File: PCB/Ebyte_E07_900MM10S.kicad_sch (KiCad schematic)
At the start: 5 parts, among them U20 ESP32-C3_OLED, U3 Ai-Thinker-Ra-02

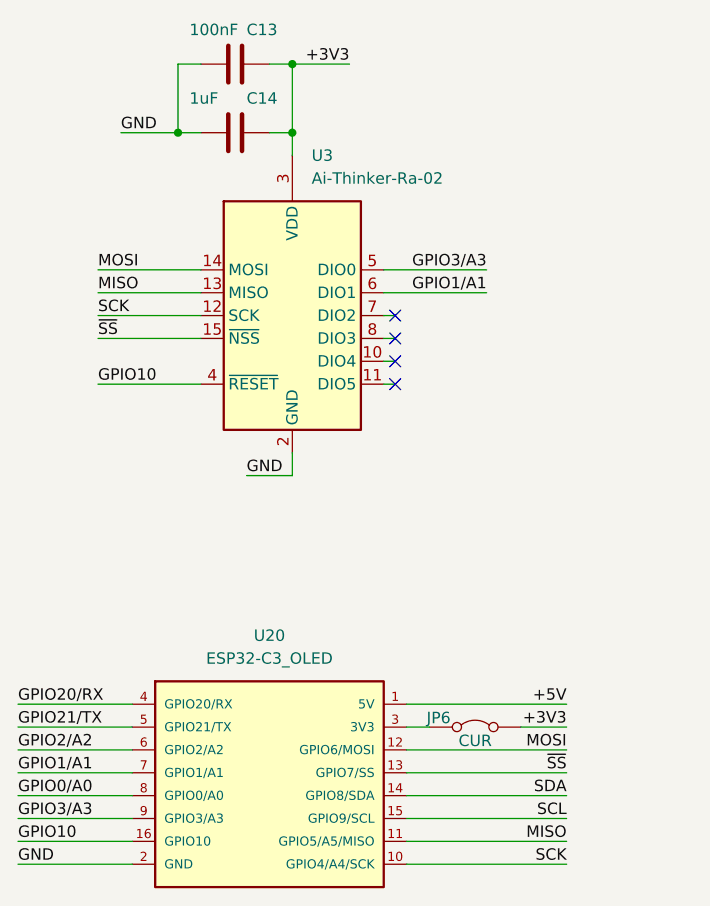
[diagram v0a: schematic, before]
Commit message: Move KiCad files to PCB
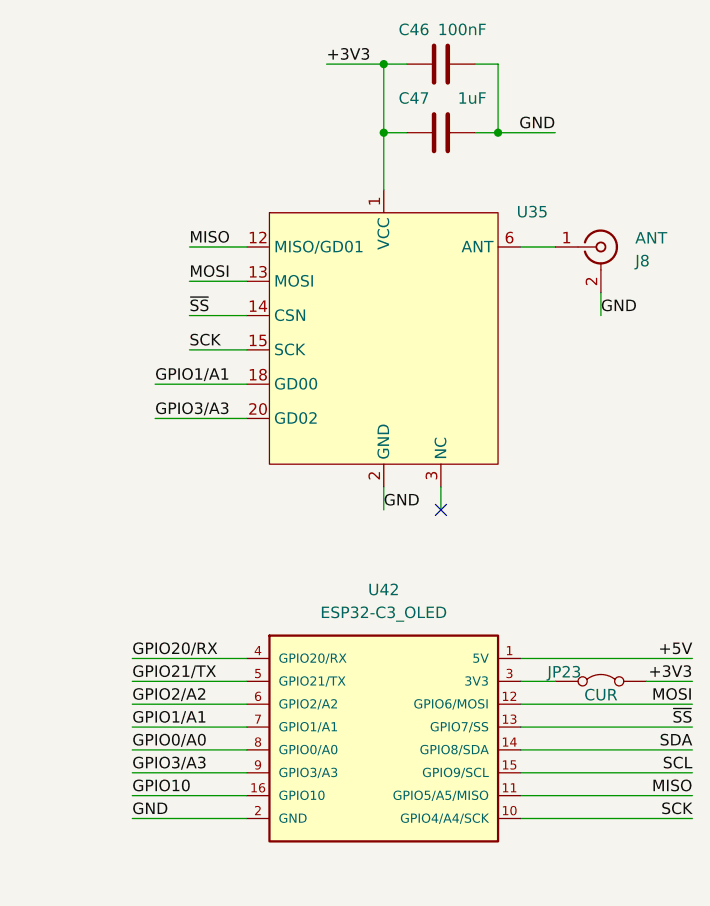
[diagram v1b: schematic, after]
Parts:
- removed C13: 100nF, Capacitor_SMD:C_0603_1608Metric, symbol Device:C
- removed C14: 1uF, Capacitor_SMD:C_0603_1608Metric, symbol Device:C
- removed JP6: CUR, Connector_PinHeader_2.54mm:PinHeader_1x02_P2.54mm_Vertical, symbol Jumper:Jumper_2_Bridged
- removed U20: ESP32-C3_OLED, module_radio:ESP32-C3_OLED, symbol module_radio:ESP32-C3_OLED
- removed U3: Ai-Thinker-Ra-02, RF_Module:Ai-Thinker-Ra-01-LoRa, symbol RF_Module:Ai-Thinker-Ra-02
- added C46: 100nF, Capacitor_SMD:C_0603_1608Metric, symbol Device:C
- added C47: 1uF, Capacitor_SMD:C_0603_1608Metric, symbol Device:C
- added J8: ANT, Connector_Coaxial:SMA_Samtec_SMA-J-P-H-ST-EM1_EdgeMount, symbol Connector:Conn_Coaxial
- added JP23: CUR, Connector_PinHeader_2.54mm:PinHeader_1x02_P2.54mm_Vertical, symbol Jumper:Jumper_2_Bridged
- added U35: Ebyte_E79, module_radio:Ebyte_E07_900MM10S, symbol module_radio:Ebyte_E07_900MM10S
- added U42: ESP32-C3_OLED, module_radio:ESP32-C3_OLED, symbol module_radio:ESP32-C3_OLED
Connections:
- net +3V3: now also C46.1, C47.1, JP23.2 (B), U35.1 (VCC)
- net +5V: now also U42.1 (5V)
- net GND: now also C46.2, C47.2, J8.2 (Ext), U35.16 (GND), U35.2 (GND), U35.7 (GND), U42.2 (GND)
- net GPIO0/A0: now also U42.8 (GPIO0/A0)
- net GPIO1/A1: now also U42.7 (GPIO1/A1)
- net GPIO10: now also U42.16 (GPIO10)
- net GPIO1/A1: now also U35.18 (GD00)
- net GPIO2/A2: now also U42.6 (GPIO2/A2)
- net GPIO20/RX: now also U42.4 (GPIO20/RX)
- net GPIO21/TX: now also U42.5 (GPIO21/TX)
- net GPIO3/A3: now also U35.20 (GD02), U42.9 (GPIO3/A3)
- net MISO: now also U35.12 (MISO/GD01), U42.11 (GPIO5/A5/MISO)
- net MOSI: now also U35.13 (MOSI), U42.12 (GPIO6/MOSI)
- net SCK: now also U35.15 (SCK), U42.10 (GPIO4/A4/SCK)
- net SCL: now also U42.15 (GPIO9/SCL)
- net SDA: now also U42.14 (GPIO8/SDA)
- net ~{SS}: now also U35.14 (CSN), U42.13 (GPIO7/SS)
- new net: U35.10 (NC), U35.11 (NC), U35.17 (NC), U35.19 (NC), U35.3 (NC), U35.4 (NC), U35.5 (NC), U35.8 (NC), U35.9 (NC)
- new net: J8.1 (In), U35.6 (ANT)
- new net: JP23.1 (A), U42.3 (3V3)
- no-connect marks 4 -> 1
